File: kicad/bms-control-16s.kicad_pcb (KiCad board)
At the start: 2 copper layers, 115 x 65 mm, 126 parts, among them J1 RJ45, J11 Conn_01x06, J2 UEXT, J3 USB_B_Micro, J4 RJ45, J5 Conn_02x09_Top_Bottom, P5 CONN_01X02, Q1 FCX495TA, T11 BC846B, T12 BC846B, U1 TPS560430X, U2 TCAN334, U3 STM32G0B1CETxN, U4 BQ76952, U5 ESP32-C3-MINI-1, U6 24AA32, U7 ESP32-WROOM-32D, Y1 8MHz

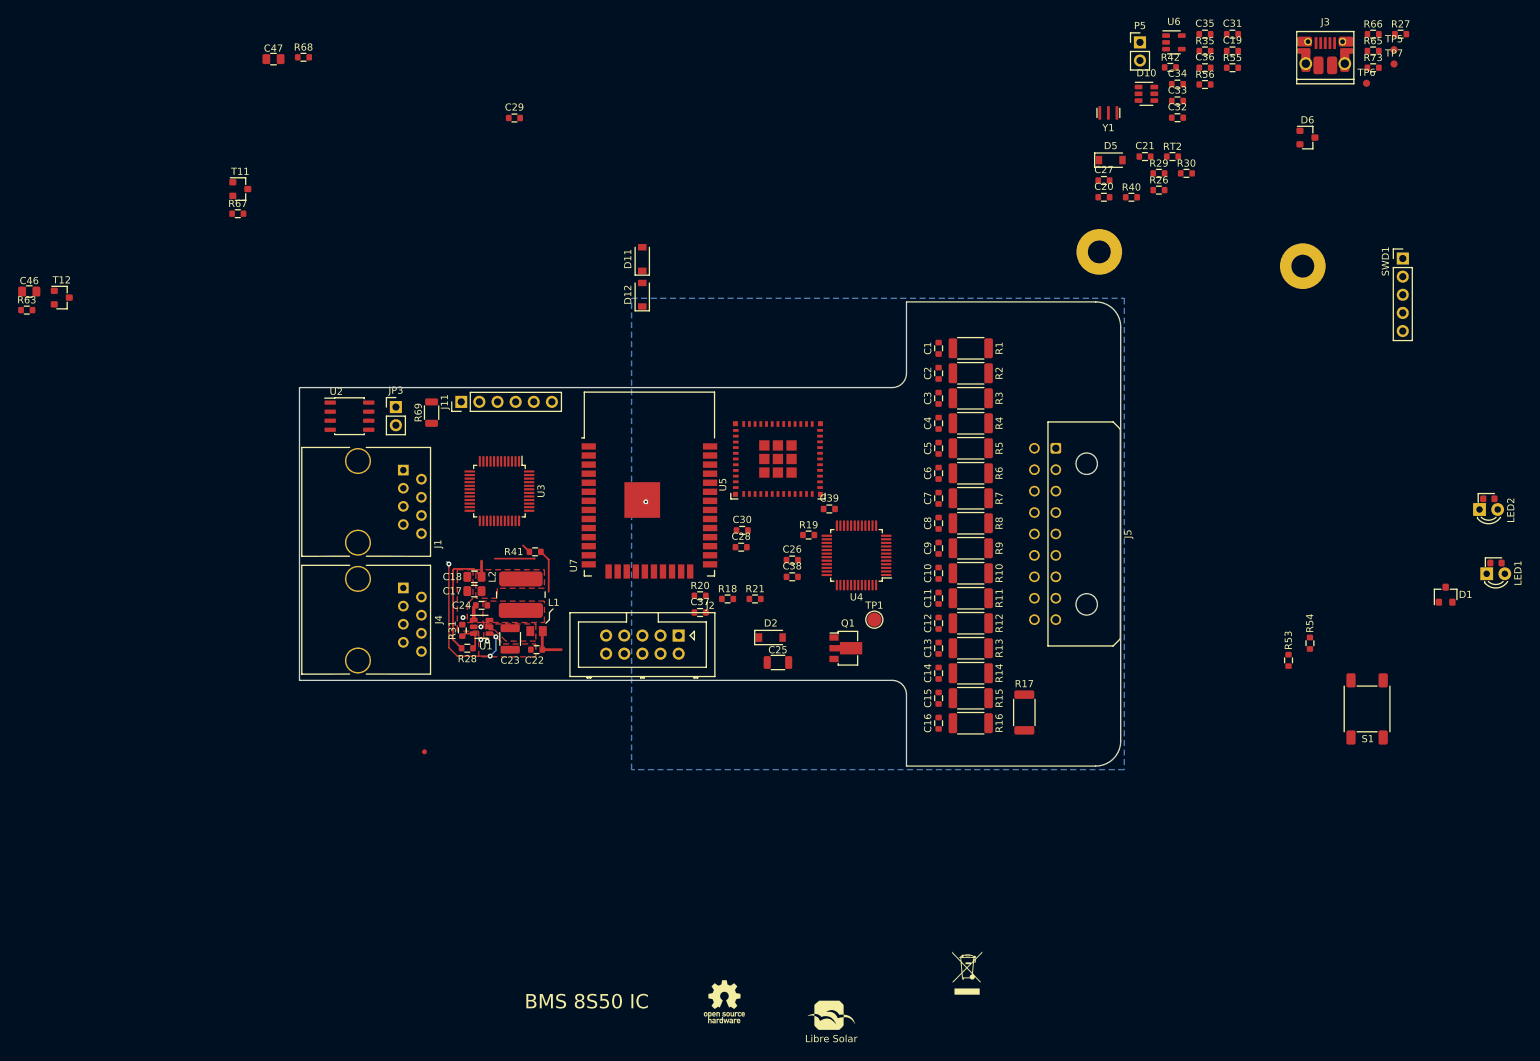
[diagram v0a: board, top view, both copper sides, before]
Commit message: Update KiCad files based on spec updates
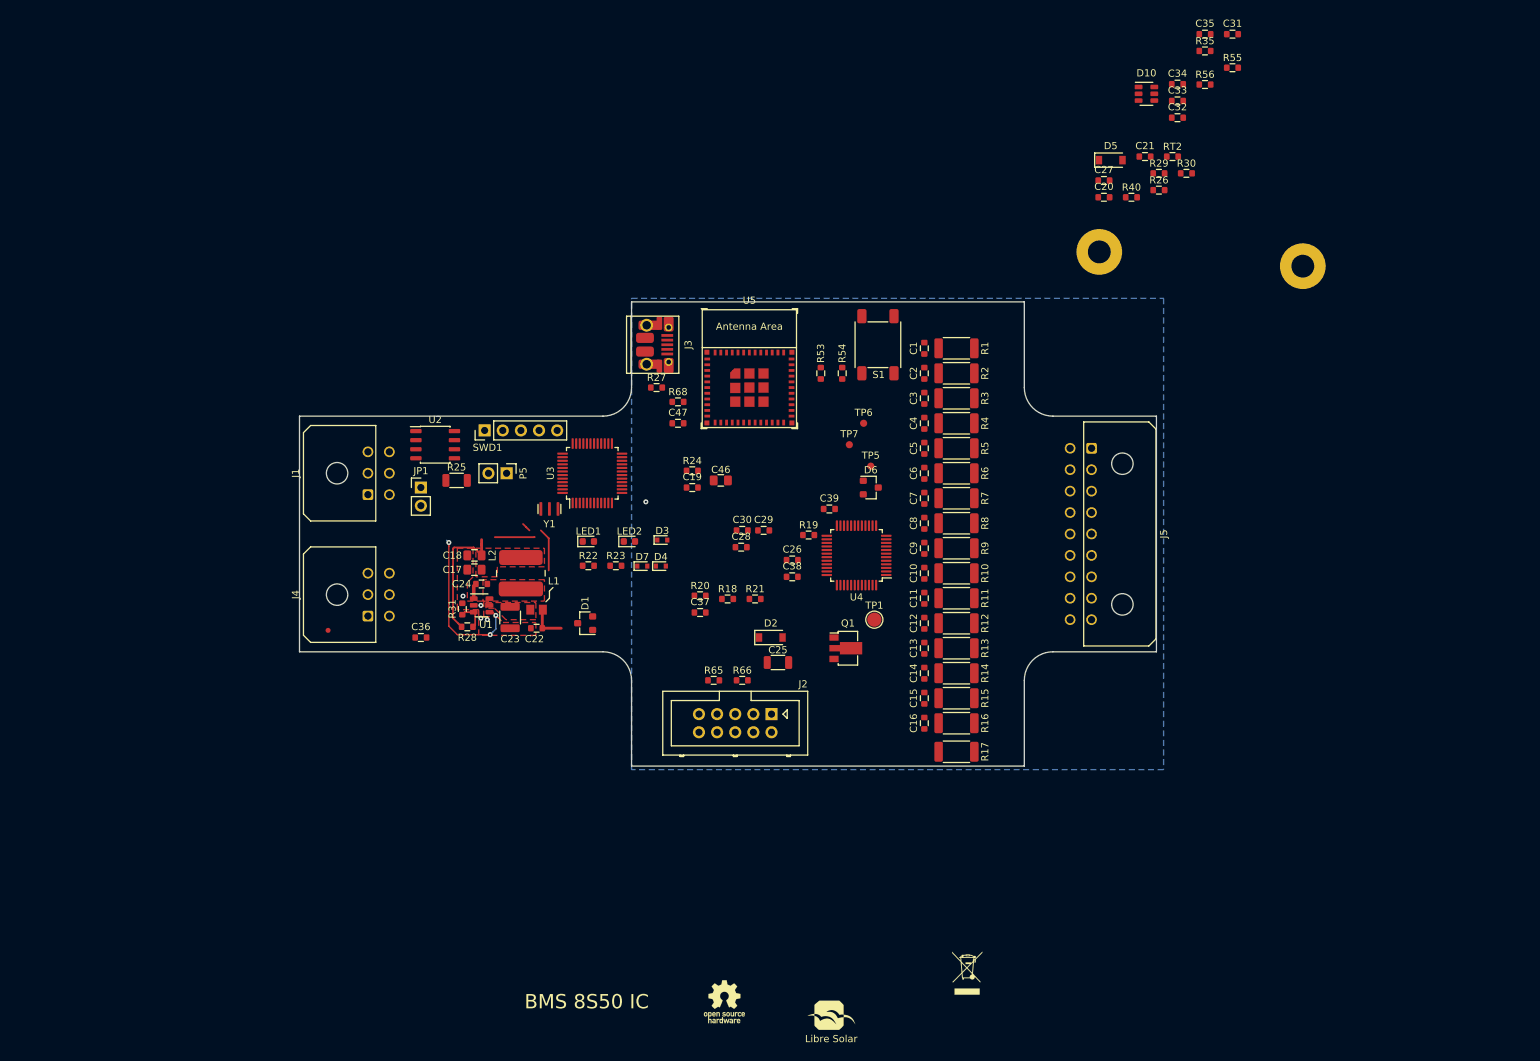
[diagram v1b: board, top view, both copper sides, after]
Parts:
- removed D11, D12: NRVTS260ESFT1G, Diode_SMD:D_SOD-123
- removed J11: Conn_01x06, Connector_PinHeader_2.54mm:PinHeader_1x06_P2.54mm_Vertical
- removed JP3: Jumper_NC_Small, Connector_PinHeader_2.54mm:PinHeader_1x02_P2.54mm_Vertical
- removed R41, R42: 1k, LibreSolar:R_0603_1608
- removed R63, R67: 10k, LibreSolar:R_0603_1608
- removed R69: 120, LibreSolar:R_1206_3216
- removed R73: 330k, LibreSolar:R_0603_1608
- removed T11, T12: BC846B, LibreSolar:SOT-23
- removed U6: 24AA32, LibreSolar:SOT-23-5
- removed U7: ESP32-WROOM-32D, RF_Module:ESP32-WROOM-32
- added D3: ESD5B5.0ST1G, Diode_SMD:D_SOD-523, F.Cu at (130.8, 88.3)
- added D4: ESD5B5.0ST1G, Diode_SMD:D_SOD-523, F.Cu at (130.6, 92.0)
- added D7: ESD5B5.0ST1G, Diode_SMD:D_SOD-523, F.Cu at (128.0, 92.0)
- added JP1: Jumper_NC_Small, Connector_PinHeader_2.54mm:PinHeader_1x02_P2.54mm_Vertical, F.Cu at (97.0, 81.0)
- added R22: 1k, LibreSolar:R_0603_1608, F.Cu at (120.5, 92.0)
- added R23: 1k, LibreSolar:R_0603_1608, F.Cu at (124.3, 92.0)
- added R24: 10k, LibreSolar:R_0603_1608, F.Cu at (135.0, 78.7)
- added R25: 120, LibreSolar:R_1206_3216, F.Cu at (102.0, 80.0)
- C19: value 100n -> 100nF
- C47: value 2.2µF -> 1µF; footprint LibreSolar:C_0805_2012 -> LibreSolar:C_0603_1608
- J1: value RJ45 -> TempSensor; footprint LibreSolar:RJ45_8P8C -> Connector_Molex:Molex_Micro-Fit_3.0_43045-0600_2x03_P3.00mm_Horizontal
- J4: value RJ45 -> CAN; footprint LibreSolar:RJ45_8P8C -> Connector_Molex:Molex_Micro-Fit_3.0_43045-0600_2x03_P3.00mm_Horizontal
- LED1, LED2: footprint LibreSolar:LED_0603_D3.0mm -> LED_SMD:LED_0603_1608Metric
- U5: footprint LibreSolar:ESP32-C3-MINI-1 -> Espressif:ESP32-C3-MINI-1
- moved C36 135.7 mm to (97.0, 102.0)
- moved SWD1 130.8 mm to (105.9, 73.0), turned to 90 degrees
- moved R65 127.7 mm to (138.0, 108.0)
- moved LED1 127.1 mm to (120.5, 88.5)
- moved R66 126.5 mm to (142.0, 108.0)
- moved D1 120.6 mm to (120.0, 100.0), turned to 180 degrees
- moved LED2 120.5 mm to (126.2, 88.5)
- moved R27 115.4 mm to (130.0, 67.0)
- moved P5 107.3 mm to (109.0, 79.0), turned to -90 degrees
- moved J3 102.1 mm to (130.0, 61.0), turned to -90 degrees
- moved C46 100.4 mm to (139.0, 80.0)
- moved C19 97.3 mm to (135.0, 81.0)
- moved Y1 95.9 mm to (115.0, 84.0)
- moved TP5 93.6 mm to (160.0, 78.0)
- moved TP7 93.1 mm to (157.0, 75.0)
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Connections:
- net /STM32 MCU/I2C1_SCL renamed /UEXT_SCL
- net /STM32 MCU/I2C1_SDA renamed /UEXT_SDA
- net /STM32 MCU/SPI1_MISO renamed /UEXT_MISO
- net /STM32 MCU/SPI1_MOSI renamed /UEXT_MOSI
- net /STM32 MCU/SPI1_SCK renamed /UEXT_SCK
- C47 pad 1: /ESP32 MCU/RESET -> /ESP32 MCU/EN
- D10 pad 1: /STM32 MCU/USB_D+ -> /USB_D+
- D10 pad 3: /STM32 MCU/USB_D- -> /USB_D-
- J1 pad 1: /STM32 MCU/CAN_H -> unconnected-(J1-Pad1)
- J1 pad 2: /STM32 MCU/CAN_L -> unconnected-(J1-Pad2)
- J1 pad 3: /CAN_GND -> unconnected-(J1-Pad3)
- J1 pad 4: /CAN_V+ -> unconnected-(J1-Pad4)
- J1 pad 5: /CAN_V+ -> unconnected-(J1-Pad5)
- J1 pad 6: Net-(J1-Pad6) -> unconnected-(J1-Pad6)
- J2 pad 10: /SSEL -> /UEXT_SSEL
- J2 pad 3: /STM32 MCU/USART2_TX -> /UEXT_TX
- J2 pad 4: /STM32 MCU/USART2_RX -> /UEXT_RX
- J3 pad 2: /STM32 MCU/USB_D- -> /USB_D-
- J3 pad 3: /STM32 MCU/USB_D+ -> /USB_D+
- J4 pad 1: /STM32 MCU/CAN_H -> unconnected-(J4-Pad1)
- J4 pad 2: /STM32 MCU/CAN_L -> unconnected-(J4-Pad2)
- J4 pad 3: /CAN_GND -> unconnected-(J4-Pad3)
- J4 pad 4: /CAN_V+ -> unconnected-(J4-Pad4)
- J4 pad 5: /CAN_V+ -> unconnected-(J4-Pad5)
- J4 pad 6: Net-(J1-Pad6) -> unconnected-(J4-Pad6)
- R55 pad 1: /STM32 MCU/I2C2_SCL -> /BQ_SCL
- R56 pad 1: /STM32 MCU/I2C2_SDA -> /BQ_SDA
- R68 pad 1: /ESP32 MCU/RESET -> /ESP32 MCU/EN
- TP6 pad 1: /STM32 MCU/I2C2_SDA -> /BQ_SDA
- TP7 pad 1: /STM32 MCU/I2C2_SCL -> /BQ_SCL
- U2 pad 1: /STM32 MCU/CAN_TX -> /CAN_TX
- U2 pad 4: /STM32 MCU/CAN_RX -> /CAN_RX
- U2 pad 6: /STM32 MCU/CAN_L -> /CAN interface/CAN_L
- U2 pad 7: /STM32 MCU/CAN_H -> /CAN interface/CAN_H
- U2 pad 8: /STM32 MCU/CAN_STB -> /CAN_STB
- U3 pad 1: /STM32 MCU/LED1 -> /LED_GREEN
- U3 pad 12: /STM32 MCU/SW_POWER -> /SW_PWR
- U3 pad 13: /STM32 MCU/USART2_TX -> /UEXT_TX
- U3 pad 14: /STM32 MCU/USART2_RX -> /UEXT_RX
- U3 pad 19: /STM32 MCU/SPI1_NSS -> /UEXT_SSEL
- U3 pad 2: /STM32 MCU/LED2 -> /LED_RED
- U3 pad 22: /STM32 MCU/I2C2_SCL -> /BQ_SCL
- U3 pad 23: /STM32 MCU/I2C2_SDA -> /BQ_SDA
- U3 pad 38: /STM32 MCU/CAN_RX -> /CAN_RX
- U3 pad 39: /STM32 MCU/CAN_TX -> /CAN_TX
- U3 pad 40: /STM32 MCU/CAN_STB -> /CAN_STB
- U3 pad 47: /STM32 MCU/ALERT_IN -> /ALERT
- U4 pad 41: unconnected-(U4-Pad41) -> /BQ76952/LD
- U4 pad 42: unconnected-(U4-Pad42) -> /BQ76952/PACK
- U5 pad 1: unconnected-(U5-Pad1) -> GND
- U5 pad 12: unconnected-(U5-Pad12) -> /LED_GREEN
- U5 pad 13: unconnected-(U5-Pad13) -> /LED_RED
- U5 pad 16: unconnected-(U5-Pad16) -> /CAN_STB
- U5 pad 18: unconnected-(U5-Pad18) -> /CAN_RX
- U5 pad 19: unconnected-(U5-Pad19) -> /CAN_TX
- U5 pad 20: unconnected-(U5-Pad20) -> /BQ_SDA
- U5 pad 21: unconnected-(U5-Pad21) -> /BQ_SCL
- U5 pad 22: unconnected-(U5-Pad22) -> Net-(R24-Pad1)
- U5 pad 23: unconnected-(U5-Pad23) -> /ESP32 MCU/BOOT
- U5 pad 24: (no net) -> unconnected-(U5-Pad24)
- U5 pad 25: (no net) -> unconnected-(U5-Pad25)
- U5 pad 26: unconnected-(U5-Pad26) -> /USB_D-
- U5 pad 27: unconnected-(U5-Pad27) -> /USB_D+
- U5 pad 28: (no net) -> unconnected-(U5-Pad28)
- U5 pad 29: (no net) -> unconnected-(U5-Pad29)
- U5 pad 3: unconnected-(U5-Pad3) -> +3V3
- U5 pad 30: unconnected-(U5-Pad30) -> /UEXT_RX
- U5 pad 31: unconnected-(U5-Pad31) -> /UEXT_TX
- U5 pad 36: (no net) -> GND
- U5 pad 5: unconnected-(U5-Pad5) -> /ALERT
- U5 pad 6: unconnected-(U5-Pad6) -> /SW_PWR
- U5 pad 8: unconnected-(U5-Pad8) -> /ESP32 MCU/EN
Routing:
- net /STM32 MCU/LED1: track 1.27 -> 0.00 mm
- net (no net): track 0.00 -> 1.27 mm
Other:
- board size 115 x 65 mm -> 120 x 65 mm

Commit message: WIP: Schematic almost finished
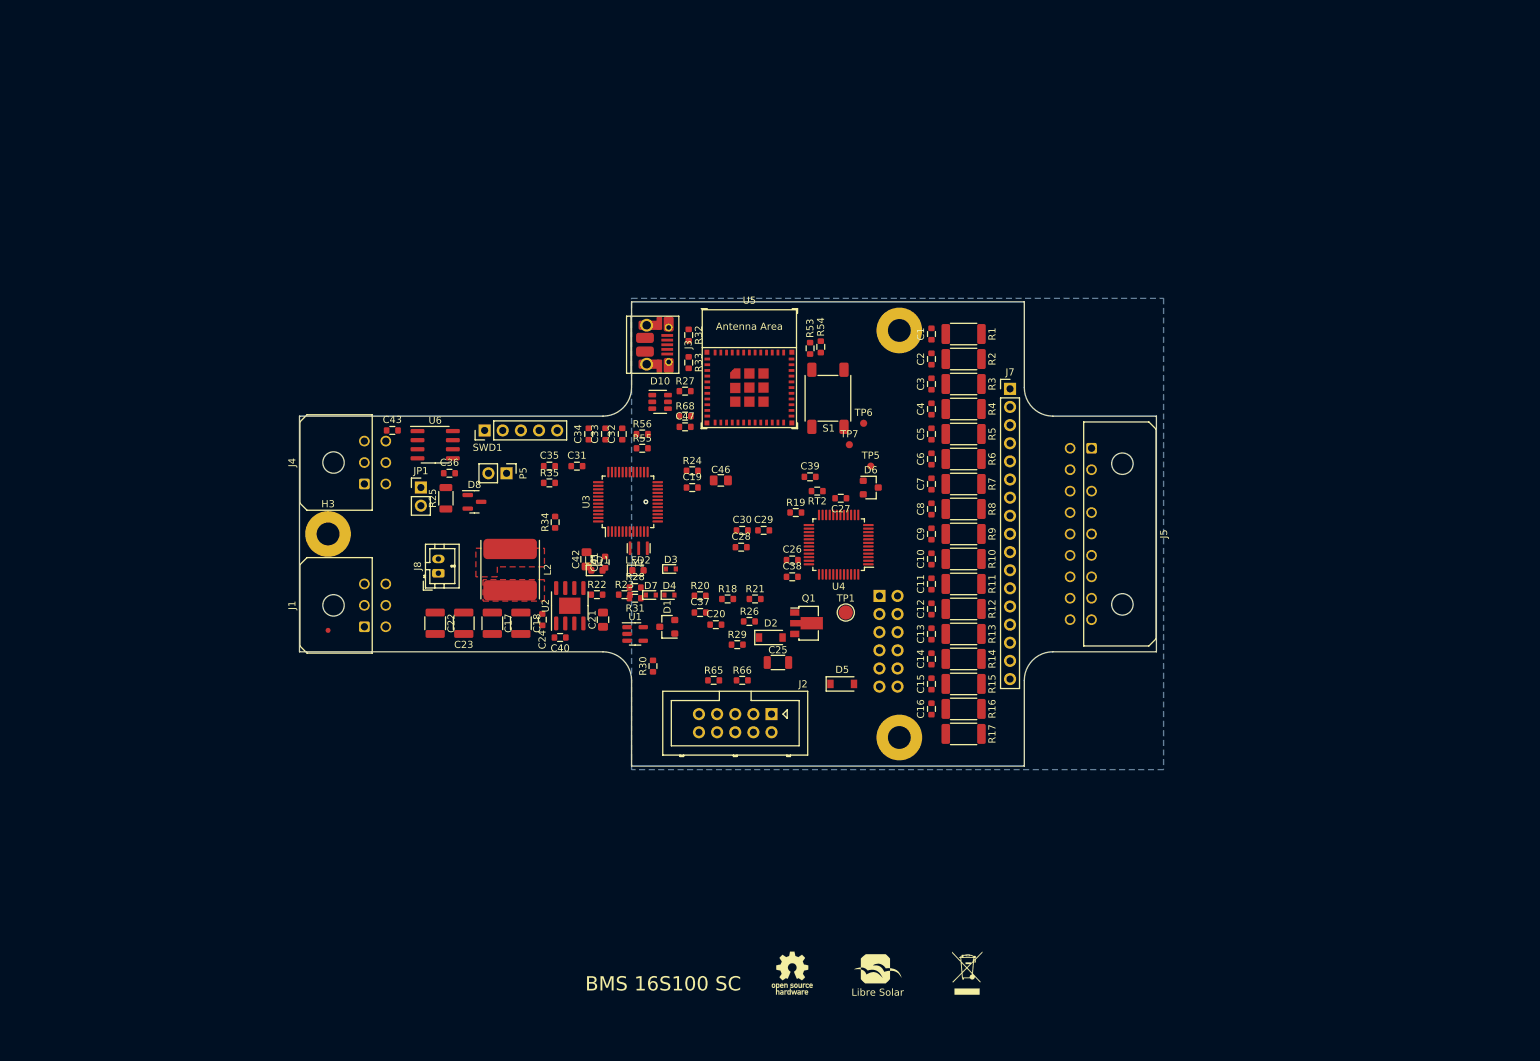
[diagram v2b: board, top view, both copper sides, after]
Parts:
- removed L1: 4.7uH, Inductor_SMD:L_0805_2012Metric
- removed R40: 22k, LibreSolar:R_0603_1608
- added C40: 100n, LibreSolar:C_0603_1608, F.Cu at (116.5, 102.0)
- added C41: 100p, LibreSolar:C_0603_1608, F.Cu at (122.8, 91.5)
- added C42: 2.2µ, LibreSolar:C_0805_2012, F.Cu at (120.2, 91.0)
- added C43: 100n, LibreSolar:C_0603_1608, F.Cu at (93.0, 73.0)
- added D8: PESD2CANFD, Package_TO_SOT_SMD:SOT-23, F.Cu at (104.5, 83.0)
- added H3: MountingHole, MountingHole:MountingHole_3.2mm_M3_Pad, F.Cu at (84.0, 87.5)
- added J6: Conn_02x06_Odd_Even, Connector_PinSocket_2.54mm:PinSocket_2x06_P2.54mm_Vertical, B.Cu at (161.2, 96.2)
- added J7: Conn_01x17, Connector_PinHeader_2.54mm:PinHeader_1x17_P2.54mm_Vertical, F.Cu at (179.5, 67.2)
- added J8: Conn_01x02, Connector_JST:JST_PH_B2B-PH-K_1x02_P2.00mm_Vertical, F.Cu at (99.5, 93.0)
- added R32: 0R, LibreSolar:R_0603_1608, F.Cu at (134.5, 59.6)
- added R33: 0R, LibreSolar:R_0603_1608, F.Cu at (134.5, 63.5)
- added R34: 49.9k, LibreSolar:R_0603_1608, F.Cu at (115.8, 85.8)
- added U6: TJA1042T-3, Package_SO:SOIC-8_3.9x4.9mm_P1.27mm, F.Cu at (99.0, 75.0)
- C17, C18: value 10u -> 47µ; footprint LibreSolar:C_0805_2012 -> LibreSolar:C_1210_3225
- C20: value 1u -> 2.2µF
- C21: value 1u -> 2.2µ; footprint LibreSolar:C_0603_1608 -> LibreSolar:C_0805_2012
- C22: value 1u -> 2.2µ; footprint LibreSolar:C_0603_1608 -> LibreSolar:C_1210_3225
- C23: value 4.7u -> 2.2µ
- J1: value TempSensor -> TempBtn
- L2: value 47uH -> 10µH; footprint LibreSolar:Bourns_SRN6045TA -> LibreSolar:Bourns_SRN8040TA
- R26: value 10k -> 1M
- R28: value 50.5k -> 100k
- R29: value 22k -> 10k
- R31: value 22k -> 17.8k
- U1: value TPS560430X -> AP2210-3.3; footprint LibreSolar:SOT-23-6 -> Package_TO_SOT_SMD:SOT-23-5
- U2: value TCAN334 -> LMR16030; footprint LibreSolar:SOIC-8_3.9x4.9mm_Pitch1.27mm -> Package_SO:SOIC-8-1EP_3.9x4.9mm_P1.27mm_EP2.29x3mm
- moved C31 109.9 mm to (118.8, 78.0)
- moved C35 109.9 mm to (115.0, 78.0)
- moved R35 109.9 mm to (115.0, 80.3)
- moved R30 101.7 mm to (129.5, 106.0), turned to 90 degrees
- moved C21 99.8 mm to (122.5, 99.5), turned to 90 degrees
- moved R55 98.3 mm to (128.0, 75.5)
- moved C34 95.9 mm to (120.5, 73.5), turned to 90 degrees
- moved R56 92.8 mm to (128.0, 73.5)
- moved C33 92.7 mm to (122.8, 73.5), turned to 90 degrees
- moved C32 89.5 mm to (125.2, 73.5), turned to 90 degrees
- moved R29 88.6 mm to (141.3, 103.0)
- moved H2 86.9 mm to (164.0, 116.0)
- moved R26 83.3 mm to (143.0, 99.8)
- moved D5 82.4 mm to (156.0, 108.5)
- moved C20 80.8 mm to (138.3, 100.2)
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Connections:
- net Net-(C25-Pad1) renamed /BQ76952/BAT
- net Net-(C27-Pad1) renamed /BQ76952/SRP
- net Net-(C27-Pad2) renamed /BQ76952/SRN
- net Net-(C30-Pad1) renamed /BQ76952/CP1
- net Net-(C37-Pad1) renamed /BQ76952/REG1
- net Net-(C38-Pad1) renamed /BQ76952/REGIN
- net Net-(Q1-Pad1) renamed /BQ76952/BREG
- C17 pad 1: +3V3 -> +5V
- C18 pad 1: +3V3 -> +5V
- C20 pad 1: unconnected-(C20-Pad1) -> Net-(C20-Pad1)
- C21 pad 1: unconnected-(C21-Pad1) -> +5V
- C22 pad 1: Net-(C22-Pad1) -> /Power Supply/VIN
- C36 pad 1: +3V3 -> +5V
- D1 pad 2: +5V -> unconnected-(D1-Pad2)
- D1 pad 3: Net-(C22-Pad1) -> /Power Supply/VIN
- D2 pad 1: unconnected-(D2-Pad1) -> Net-(D2-Pad1)
- D2 pad 2: unconnected-(D2-Pad2) -> /CHG+
- D3 pad 2: /USB_D- -> Net-(D3-Pad2)
- D4 pad 2: /USB_D+ -> Net-(D4-Pad2)
- J1 pad 1: unconnected-(J1-Pad1) -> /TEMP1
- J1 pad 2: unconnected-(J1-Pad2) -> /TEMP2
- J1 pad 3: unconnected-(J1-Pad3) -> /BTN_1
- J1 pad 4: unconnected-(J1-Pad4) -> GND
- J1 pad 5: unconnected-(J1-Pad5) -> GND
- J1 pad 6: unconnected-(J1-Pad6) -> /BTN_2
- J3 pad 2: /USB_D- -> Net-(D3-Pad2)
- J3 pad 3: /USB_D+ -> Net-(D4-Pad2)
- J4 pad 1: unconnected-(J4-Pad1) -> /CAN_H
- J4 pad 2: unconnected-(J4-Pad2) -> /CAN_L
- J4 pad 3: unconnected-(J4-Pad3) -> GND
- J4 pad 4: unconnected-(J4-Pad4) -> /CAN_H
- J4 pad 5: unconnected-(J4-Pad5) -> /CAN_L
- J4 pad 6: unconnected-(J4-Pad6) -> GND
- JP1 pad 1: /CAN interface/CAN_H -> /CAN_H
- L2 pad 2: +3V3 -> +5V
- R19 pad 1: /BQ76952/BAT- -> /BAT-
- R20 pad 1: /BQ76952/PGND -> /PGND
- R21 pad 2: unconnected-(R21-Pad2) -> Net-(D2-Pad1)
- R25 pad 2: /CAN interface/CAN_L -> /CAN_L
- R26 pad 1: GND -> /ALERT
- R26 pad 2: /BQ76952/XT2 -> +3V3
- R28 pad 1: +3V3 -> +5V
- R29 pad 1: /BQ76952/NTC_BAT -> /BQ76952/PACK
- R29 pad 2: /BQ76952/TEMPO -> /PACK+
- R30 pad 1: GND -> /BQ76952/LD
- R30 pad 2: /BQ76952/NTC_BAT -> /PACK+
- R53 pad 2: /BQ76952/BTN_SIGNAL -> /SW_PWR
- R54 pad 1: /BQ76952/BTN_SIGNAL -> /SW_PWR
- R54 pad 2: /BQ76952/BTN_2 -> /BTN_2
- R55 pad 1: /BQ_SCL -> /BQ_SCK_SCL
- R56 pad 1: /BQ_SDA -> /BQ_MISO_SDA
- RT2 pad 1: /BQ76952/XT2 -> /BQ76952/TS3
- S1 pad 1: /BQ76952/BTN_2 -> /BTN_2
- S1 pad 2: /BQ76952/WAKE -> /BTN_1
- TP6 pad 1: /BQ_SDA -> /BQ_MISO_SDA
- TP7 pad 1: /BQ_SCL -> /BQ_SCK_SCL
- U1 pad 1: Net-(C24-Pad1) -> +5V
- U1 pad 3: /Power Supply/FB -> +5V
- U1 pad 4: /Power Supply/EN -> Net-(C41-Pad1)
- U1 pad 5: /Power Supply/VIN -> +3V3
- U2 pad 1: /CAN_TX -> Net-(C24-Pad1)
- U2 pad 2: GND -> /Power Supply/VIN
- U2 pad 3: +3V3 -> /Power Supply/EN
- U2 pad 4: /CAN_RX -> Net-(R34-Pad1)
- U2 pad 5: unconnected-(U2-Pad5) -> /Power Supply/FB
- U2 pad 6: /CAN interface/CAN_L -> /Power Supply/PGOOD
- U2 pad 7: /CAN interface/CAN_H -> GND
- U2 pad 8: /CAN_STB -> /Power Supply/SW
- U3 pad 22: /BQ_SCL -> unconnected-(U3-Pad22)
- U3 pad 23: /BQ_SDA -> unconnected-(U3-Pad23)
- U3 pad 24: /STM32 MCU/SPI2_NSS -> /BQ_NSS
- U3 pad 25: /STM32 MCU/SPI2_SCK -> /BQ_SCK_SCL
- U3 pad 26: /STM32 MCU/SPI2_MISO -> /BQ_MISO_SDA
- U3 pad 27: /STM32 MCU/SPI2_MOSI -> /BQ_MOSI
- U4 pad 21: /BQ76952/TS1 -> /TEMP1
- U4 pad 22: /BQ76952/WAKE -> /BTN_1
- U4 pad 24: unconnected-(U4-Pad24) -> Net-(C20-Pad1)
- U4 pad 25: unconnected-(U4-Pad25) -> /ALERT
- U4 pad 26: unconnected-(U4-Pad26) -> /BQ_SCK_SCL
- U4 pad 27: unconnected-(U4-Pad27) -> /BQ_MISO_SDA
- U4 pad 28: unconnected-(U4-Pad28) -> /BQ_MOSI
- U4 pad 29: unconnected-(U4-Pad29) -> /BQ_NSS
- U4 pad 30: unconnected-(U4-Pad30) -> /TEMP2
- U4 pad 31: unconnected-(U4-Pad31) -> /TEMP4
- U4 pad 33: unconnected-(U4-Pad33) -> /BQ76952/RST_SHUT
- U4 pad 38: unconnected-(U4-Pad38) -> GND
- U4 pad 39: /BQ76952/PDSG -> /PDSG
- U4 pad 43: /BQ76952/DSG -> /DSG
- U4 pad 45: /BQ76952/CHG -> /CHG
- U5 pad 20: /BQ_SDA -> /BQ_MISO_SDA
- U5 pad 21: /BQ_SCL -> /BQ_SCK_SCL
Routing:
- net /Power Supply/EN: track 22.6 -> 0.00 mm, vias 3 -> 0
- net +3V3: track 18.2 -> 0.00 mm
- net Net-(LED1-Pad2): track 6.07 -> 0.00 mm
- net +5V: track 5.59 -> 0.00 mm
- net Net-(C22-Pad1): track 5.45 -> 0.00 mm
- net /Power Supply/FB: track 4.00 -> 0.00 mm
- net Net-(C24-Pad1): track 2.17 -> 0.00 mm
- net (no net): track 1.27 -> 0.00 mm
- net GND: vias 5 -> 1
- removed copper zone on F.Cu, net /Power Supply/VIN
- removed copper zone on F.Cu, net GND
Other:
- board text added: "BMS 16S100 SC"
- board text removed: "BMS 8S50 IC"
